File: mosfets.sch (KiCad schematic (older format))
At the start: 45 parts, among them Q1 ZXTC2045E6, Q10 ZXTC2045E6, Q11 IXFK230N20T, Q12 IXFK230N20T, Q2 ZXTC2045E6, Q3 IXFK230N20T, Q4 IXFK230N20T, Q5 ZXTC2045E6, Q6 ZXTC2045E6, Q7 IXFK230N20T, Q8 IXFK230N20T, Q9 ZXTC2045E6

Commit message: ~ changed gate resistance to 1R ~ changed power mosfet to IRFP4668PBF
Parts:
- Q11, Q12, Q3, Q4, Q7, Q8: value IXFK230N20T -> IRFP4668PBF
- R16, R17, R22, R23, R28, R29: value 4R7 -> 1R
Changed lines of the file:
@@
 LIBS:contrib
 LIBS:valves
-LIBS:alexlib
 LIBS:HSWR V2-cache
 EELAYER 25 0
@@
 P 9550 4750
 F 0 "R29" V 9630 4750 50  0000 C CNN
-F 1 "4R7" V 9550 4750 50  0000 C CNN
+F 1 "1R" V 9550 4750 50  0000 C CNN
 F 2 "Resistors_SMD:R_0805" V 9480 4750 50  0001 C CNN
 F 3 "" H 9550 4750 50  0000 C CNN
@@
 P 9550 2600
 F 0 "R28" V 9630 2600 50  0000 C CNN
-F 1 "4R7" V 9550 2600 50  0000 C CNN
+F 1 "1R" V 9550 2600 50  0000 C CNN
 F 2 "Resistors_SMD:R_0805" V 9480 2600 50  0001 C CNN
 F 3 "" H 9550 2600 50  0000 C CNN
@@
 P 9950 4750
 F 0 "Q12" H 10250 4800 50  0000 R CNN
-F 1 "IXFK230N20T" H 10600 4700 50  0000 R CNN
+F 1 "IRFP4668PBF" H 10600 4700 50  0000 R CNN
 F 2 "alexmod:TO-264_flat_reverse" H 10150 4850 29  0001 C CNN
 F 3 "" H 9950 4750 60  0000 C CNN
@@
 P 9950 2600
 F 0 "Q11" H 10250 2650 50  0000 R CNN
-F 1 "IXFK230N20T" H 10600 2550 50  0000 R CNN
+F 1 "IRFP4668PBF" H 10600 2550 50  0000 R CNN
 F 2 "alexmod:TO-264_flat_reverse" H 10150 2700 29  0001 C CNN
 F 3 "" H 9950 2600 60  0000 C CNN
@@
 P 6100 4750
 F 0 "R23" V 6180 4750 50  0000 C CNN
-F 1 "4R7" V 6100 4750 50  0000 C CNN
+F 1 "1R" V 6100 4750 50  0000 C CNN
 F 2 "Resistors_SMD:R_0805" V 6030 4750 50  0001 C CNN
 F 3 "" H 6100 4750 50  0000 C CNN
@@
 P 6100 2600
 F 0 "R22" V 6180 2600 50  0000 C CNN
-F 1 "4R7" V 6100 2600 50  0000 C CNN
+F 1 "1R" V 6100 2600 50  0000 C CNN
 F 2 "Resistors_SMD:R_0805" V 6030 2600 50  0001 C CNN
 F 3 "" H 6100 2600 50  0000 C CNN
@@
 P 6500 4750
 F 0 "Q8" H 6800 4800 50  0000 R CNN
-F 1 "IXFK230N20T" H 7150 4700 50  0000 R CNN
+F 1 "IRFP4668PBF" H 7150 4700 50  0000 R CNN
 F 2 "alexmod:TO-264_flat_reverse" H 6700 4850 29  0001 C CNN
 F 3 "" H 6500 4750 60  0000 C CNN
@@
 P 6500 2600
 F 0 "Q7" H 6800 2650 50  0000 R CNN
-F 1 "IXFK230N20T" H 7150 2550 50  0000 R CNN
+F 1 "IRFP4668PBF" H 7150 2550 50  0000 R CNN
 F 2 "alexmod:TO-264_flat_reverse" H 6700 2700 29  0001 C CNN
 F 3 "" H 6500 2600 60  0000 C CNN
@@
 P 2700 4750
 F 0 "R17" V 2780 4750 50  0000 C CNN
-F 1 "4R7" V 2700 4750 50  0000 C CNN
+F 1 "1R" V 2700 4750 50  0000 C CNN
 F 2 "Resistors_SMD:R_0805" V 2630 4750 50  0001 C CNN
 F 3 "" H 2700 4750 50  0000 C CNN
@@
 P 2700 2600
 F 0 "R16" V 2780 2600 50  0000 C CNN
-F 1 "4R7" V 2700 2600 50  0000 C CNN
+F 1 "1R" V 2700 2600 50  0000 C CNN
 F 2 "Resistors_SMD:R_0805" V 2630 2600 50  0001 C CNN
 F 3 "" H 2700 2600 50  0000 C CNN
@@
 P 3050 4750
 F 0 "Q4" H 3350 4800 50  0000 R CNN
-F 1 "IXFK230N20T" H 3700 4700 50  0000 R CNN
+F 1 "IRFP4668PBF" H 3700 4700 50  0000 R CNN
 F 2 "alexmod:TO-264_flat_reverse" H 3250 4850 29  0001 C CNN
 F 3 "" H 3050 4750 60  0000 C CNN
@@
 P 3050 2600
 F 0 "Q3" H 3350 2650 50  0000 R CNN
-F 1 "IXFK230N20T" H 3700 2550 50  0000 R CNN
+F 1 "IRFP4668PBF" H 3700 2550 50  0000 R CNN
 F 2 "alexmod:TO-264_flat_reverse" H 3250 2700 29  0001 C CNN
 F 3 "" H 3050 2600 60  0000 C CNN

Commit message: - updated project to 5.0.0 - added ignore file
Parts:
- C3, C4, C5, C52, C54, C55, C56, C57, C58, C6, C7, C8: symbol C -> Device:C
- C50, C51, C53: symbol CP -> Device:CP
- Q1, Q10, Q2, Q5, Q6, Q9: symbol ZXTC2045E6 -> HSWR-V2-rescue:ZXTC2045E6
- Q11, Q12, Q3, Q4, Q7, Q8: symbol Q_NMOS_GDS -> Device:Q_NMOS_GDS
- R12, R13, R14, R15, R16, R17, R18, R19, R20, R21, R22, R23, R24, R25, R26, R27, R28, R29: symbol R -> Device:R
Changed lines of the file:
@@
-EESchema Schematic File Version 2
-LIBS:HSWR V2-rescue
-LIBS:power
-LIBS:device
-LIBS:transistors
-LIBS:conn
-LIBS:linear
-LIBS:regul
-LIBS:74xx
-LIBS:cmos4000
-LIBS:adc-dac
-LIBS:memory
-LIBS:xilinx
-LIBS:microcontrollers
-LIBS:dsp
-LIBS:microchip
-LIBS:analog_switches
-LIBS:motorola
-LIBS:texas
-LIBS:intel
-LIBS:audio
-LIBS:interface
-LIBS:digital-audio
-LIBS:philips
-LIBS:display
-LIBS:cypress
-LIBS:siliconi
-LIBS:opto
-LIBS:atmel
-LIBS:contrib
-LIBS:valves
+EESchema Schematic File Version 4
 LIBS:HSWR V2-cache
-EELAYER 25 0
+EELAYER 26 0
 EELAYER END
 $Descr A4 11693 8268
@@
 Connection ~ 10050 3650
 $Comp
-L +BATT #PWR024
+L power:+BATT #PWR024
 U 1 1 575A4EA5
 P 10050 1700
@@
 $EndComp
 $Comp
-L R R29
+L Device:R R29
 U 1 1 57621E05
 P 9550 4750
@@
 	9750 4750 9700 4750
 $Comp
-L C C8
+L Device:C C8
 U 1 1 57621E21
 P 8200 5250
@@
 $EndComp
 $Comp
-L R R27
+L Device:R R27
 U 1 1 57621E27
 P 9350 5200
@@
 $EndComp
 $Comp
-L ZXTC2045E6 Q10
+L HSWR-V2-rescue:ZXTC2045E6 Q10
 U 1 1 57621E2D
 P 8800 4850
@@
 	8350 4400 8350 5050
 $Comp
-L R R25
+L Device:R R25
 U 1 1 57621E3C
 P 8600 4400
@@
 	10050 5400 10050 4950
 $Comp
-L R R28
+L Device:R R28
 U 1 1 576296B6
 P 9550 2600
@@
 Connection ~ 10050 3250
 $Comp
-L C C7
+L Device:C C7
 U 1 1 576296D2
 P 8200 3100
@@
 $EndComp
 $Comp
-L R R26
+L Device:R R26
 U 1 1 576296D8
 P 9350 3050
@@
 $EndComp
 $Comp
-L ZXTC2045E6 Q9
+L HSWR-V2-rescue:ZXTC2045E6 Q9
 U 1 1 576296DE
 P 8800 2700
@@
 	8350 2250 8350 2900
 $Comp
-L R R24
+L Device:R R24
 U 1 1 576296ED
 P 8600 2250
@@
 Connection ~ 8200 5400
 $Comp
-L Q_NMOS_GDS Q12
+L Device:Q_NMOS_GDS Q12
 U 1 1 57637BFB
 P 9950 4750
@@
 $EndComp
 $Comp
-L Q_NMOS_GDS Q11
+L Device:Q_NMOS_GDS Q11
 U 1 1 57637E5A
 P 9950 2600
@@
 Connection ~ 6600 3650
 $Comp
-L +BATT #PWR025
+L power:+BATT #PWR025
 U 1 1 589857E2
 P 6600 1700
@@
 $EndComp
 $Comp
-L R R23
+L Device:R R23
 U 1 1 589857E8
 P 6100 4750
@@
 	6300 4750 6250 4750
 $Comp
-L C C6
+L Device:C C6
 U 1 1 589857F0
 P 4750 5250
@@
 $EndComp
 $Comp
-L R R21
+L Device:R R21
 U 1 1 589857F7
 P 5900 5200
@@
 $EndComp
 $Comp
-L ZXTC2045E6 Q6
+L HSWR-V2-rescue:ZXTC2045E6 Q6
 U 1 1 589857FE
 P 5350 4850
@@
 	4900 4400 4900 5050
 $Comp
-L R R19
+L Device:R R19
 U 1 1 58985809
 P 5150 4400
@@
 	6600 5400 6600 4950
 $Comp
-L R R22
+L Device:R R22
 U 1 1 58985817
 P 6100 2600
@@
 Connection ~ 6600 3250
 $Comp
-L C C5
+L Device:C C5
 U 1 1 58985820
 P 4750 3100
@@
 $EndComp
 $Comp
-L R R20
+L Device:R R20
 U 1 1 58985827
 P 5900 3050
@@
 $EndComp
 $Comp
-L ZXTC2045E6 Q5
+L HSWR-V2-rescue:ZXTC2045E6 Q5
 U 1 1 5898582E
 P 5350 2700
@@
 	4900 2250 4900 2900
 $Comp
-L R R18
+L Device:R R18
 U 1 1 5898583A
 P 5150 2250
@@
 Connection ~ 4750 5400
 $Comp
-L Q_NMOS_GDS Q8
+L Device:Q_NMOS_GDS Q8
 U 1 1 5898584D
 P 6500 4750
@@
 $EndComp
 $Comp
-L Q_NMOS_GDS Q7
+L Device:Q_NMOS_GDS Q7
 U 1 1 58985854
 P 6500 2600
@@
 Connection ~ 3150 3650
 $Comp
-L +BATT #PWR026
+L power:+BATT #PWR026
 U 1 1 58986AF5
 P 3150 1700
@@
 $EndComp
 $Comp
-L R R17
+L Device:R R17
 U 1 1 58986AFB
 P 2700 4750
@@
 	2850 4750 2850 4750
 $Comp
-L C C4
+L Device:C C4
 U 1 1 58986B03
 P 1350 5250
@@
 $EndComp
 $Comp
-L R R15
+L Device:R R15
 U 1 1 58986B0A
 P 2500 5200
@@
 $EndComp
 $Comp
-L ZXTC2045E6 Q2
+L HSWR-V2-rescue:ZXTC2045E6 Q2
 U 1 1 58986B11
 P 1950 4850
@@
 	1500 4400 1500 5050
 $Comp
-L R R13
+L Device:R R13
 U 1 1 58986B1C
 P 1750 4400
@@
 	3150 5400 3150 4950
 $Comp
-L R R16
+L Device:R R16
 U 1 1 58986B2A
 P 2700 2600
@@
 Connection ~ 3150 3250
 $Comp
-L C C3
+L Device:C C3
 U 1 1 58986B33
 P 1350 3100
@@
 $EndComp
 $Comp
-L R R14
+L Device:R R14
 U 1 1 58986B3A
 P 2500 3050
@@
 $EndComp
 $Comp
-L ZXTC2045E6 Q1
+L HSWR-V2-rescue:ZXTC2045E6 Q1
 U 1 1 58986B41
 P 1950 2700
@@
 	1500 2250 1500 2900
 $Comp
-L R R12
+L Device:R R12
 U 1 1 58986B4D
 P 1750 2250
@@
 Connection ~ 1350 5400
 $Comp
-L Q_NMOS_GDS Q4
+L Device:Q_NMOS_GDS Q4
 U 1 1 58986B60
 P 3050 4750
@@
 $EndComp
 $Comp
-L Q_NMOS_GDS Q3
+L Device:Q_NMOS_GDS Q3
 U 1 1 58986B67
 P 3050 2600
@@
 	1200 5400 3800 5400
 $Comp
-L +BATT #PWR027
+L power:+BATT #PWR027
 U 1 1 58A716A6
 P 3450 7000
@@
 $EndComp
 $Comp
-L C C52
+L Device:C C52
 U 1 1 58A7831F
 P 3550 5200
@@
 $EndComp
 $Comp
-L C C54
+L Device:C C54
 U 1 1 58A78A84
 P 3800 5200
@@
 Connection ~ 3800 5050
 $Comp
-L C C55
+L Device:C C55
 U 1 1 58A797A9
 P 7000 5200
@@
 $EndComp
 $Comp
-L C C56
+L Device:C C56
 U 1 1 58A797AF
 P 7250 5200
@@
 Connection ~ 7250 5050
 $Comp
-L C C57
+L Device:C C57
 U 1 1 58A799C2
 P 10450 5200
@@
 $EndComp
 $Comp
-L C C58
+L Device:C C58
 U 1 1 58A799C8
 P 10700 5200
@@
 Connection ~ 6600 1700
 $Comp
-L CP C51
+L Device:CP C51
 U 1 1 58A7B686
 P 3450 7150
@@
 $EndComp
 $Comp
-L CP C53
+L Device:CP C53
 U 1 1 58A7B84C
 P 3700 7150
@@
 $EndComp
 $Comp
-L CP C50
+L Device:CP C50
 U 1 1 58A7B8F0
 P 3200 7150
@@
 $EndComp
 $Comp
-L GNDPWR #PWR028
+L HSWR-V2-rescue:GNDPWR #PWR028
 U 1 1 58A7BA9C
 P 3450 7300

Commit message: - updated to VESC6 architecture - still some things to do in schematic
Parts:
- removed C3, C4, C5, C6, C7, C8: 1u, Capacitors_SMD:C_0805, symbol Device:C
- removed Q1, Q10, Q2, Q5, Q6, Q9: ZXTC2045E6, TO_SOT_Packages_SMD:SOT-23-6, symbol HSWR-V2-rescue:ZXTC2045E6
- removed R12, R13, R18, R19, R24, R25: 120R, Resistors_SMD:R_0805, symbol Device:R
- removed R14, R15, R20, R21, R26, R27: 10k, Resistors_SMD:R_0805, symbol Device:R
- C50, C51, C53: footprint alexmod:C_Radial_D22_P10 -> Capacitor_THT:CP_Radial_D22.0mm_P10.00mm_SnapIn
- C52, C54, C55, C56, C57, C58: footprint Capacitors_SMD:C_2220 -> Capacitor_SMD:C_2220_5650Metric
- Q11, Q12, Q3, Q4, Q7, Q8: value IRFP4668PBF -> IXFK300N20X3; footprint alexmod:TO-264_flat_reverse -> Package_TO_SOT_THT:TO-264-3_Horizontal_TabUp
- R16, R17, R22, R23, R28, R29: footprint Resistors_SMD:R_0805 -> Resistor_SMD:R_0805_2012Metric
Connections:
- net labels added: U, U_GH, U_GL, U_VP, U_VS, V, V_GH, V_GL, V_VP, V_VS, W, W_GH, W_GL, W_VP, W_VS
- net labels removed: GNDPWR, H1_HI, H1_LOW, H1_VL, H1_VS, H2_HI, H2_LOW, H2_VL, H2_VS, H3_HI, H3_LOW, H3_VL, H3_VS, M_H1, M_H2, M_H3, M_L1, M_L2, M_L3, PHASE_1, PHASE_2, PHASE_3
- wire segments 95 -> 50

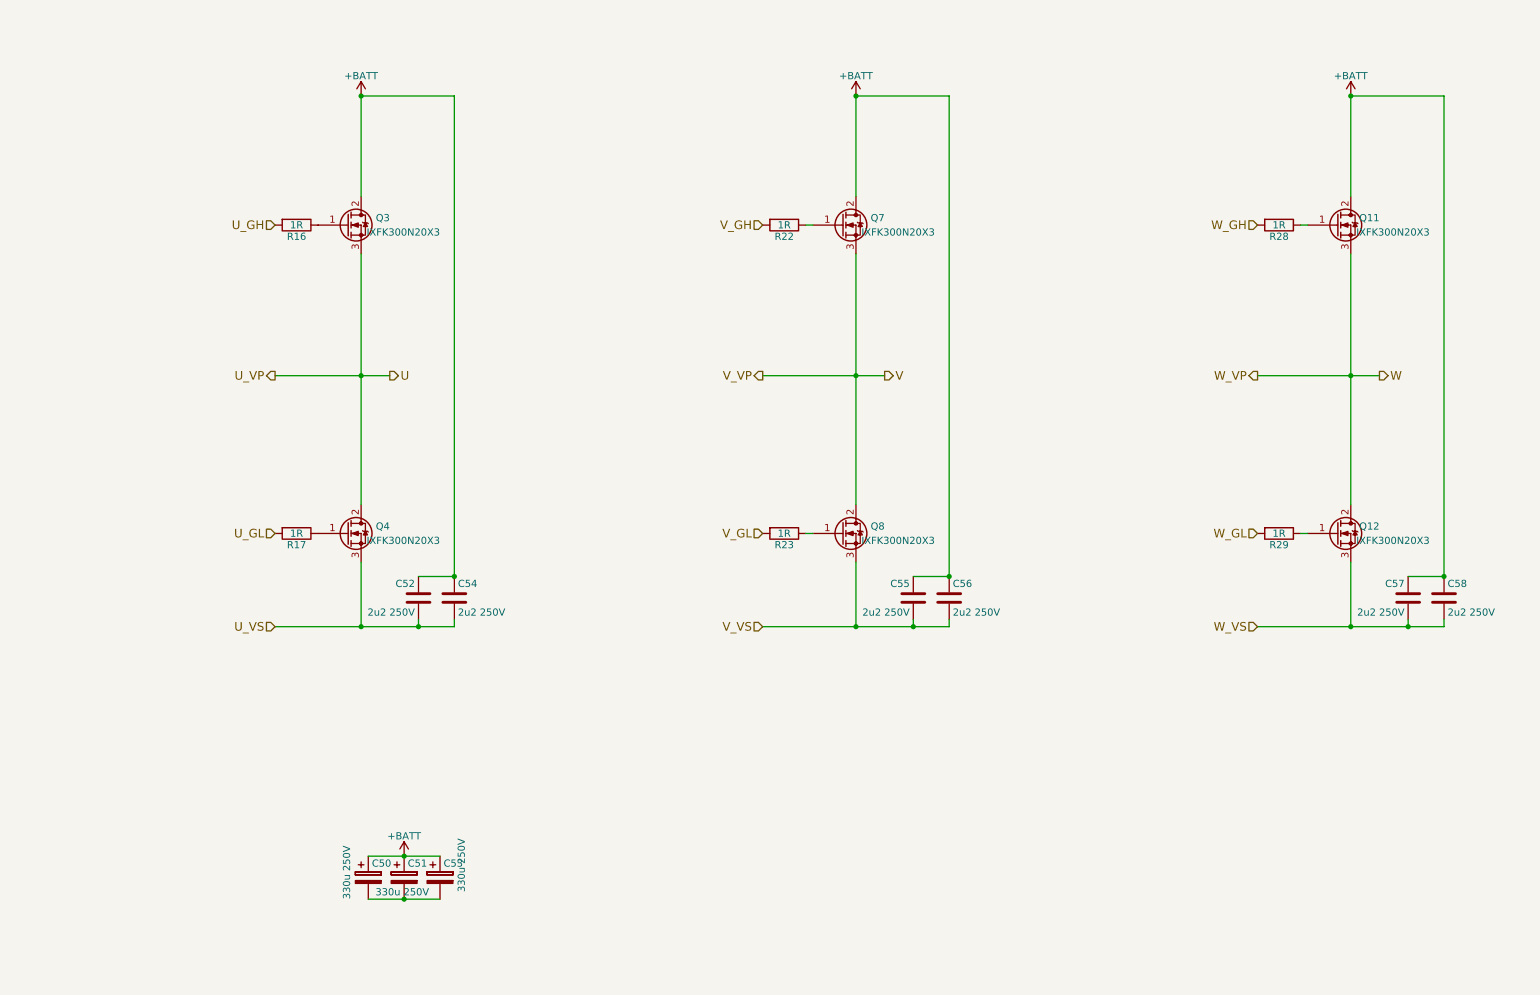
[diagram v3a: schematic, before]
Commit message: - started layout - high current path finished - some work on gate drivers
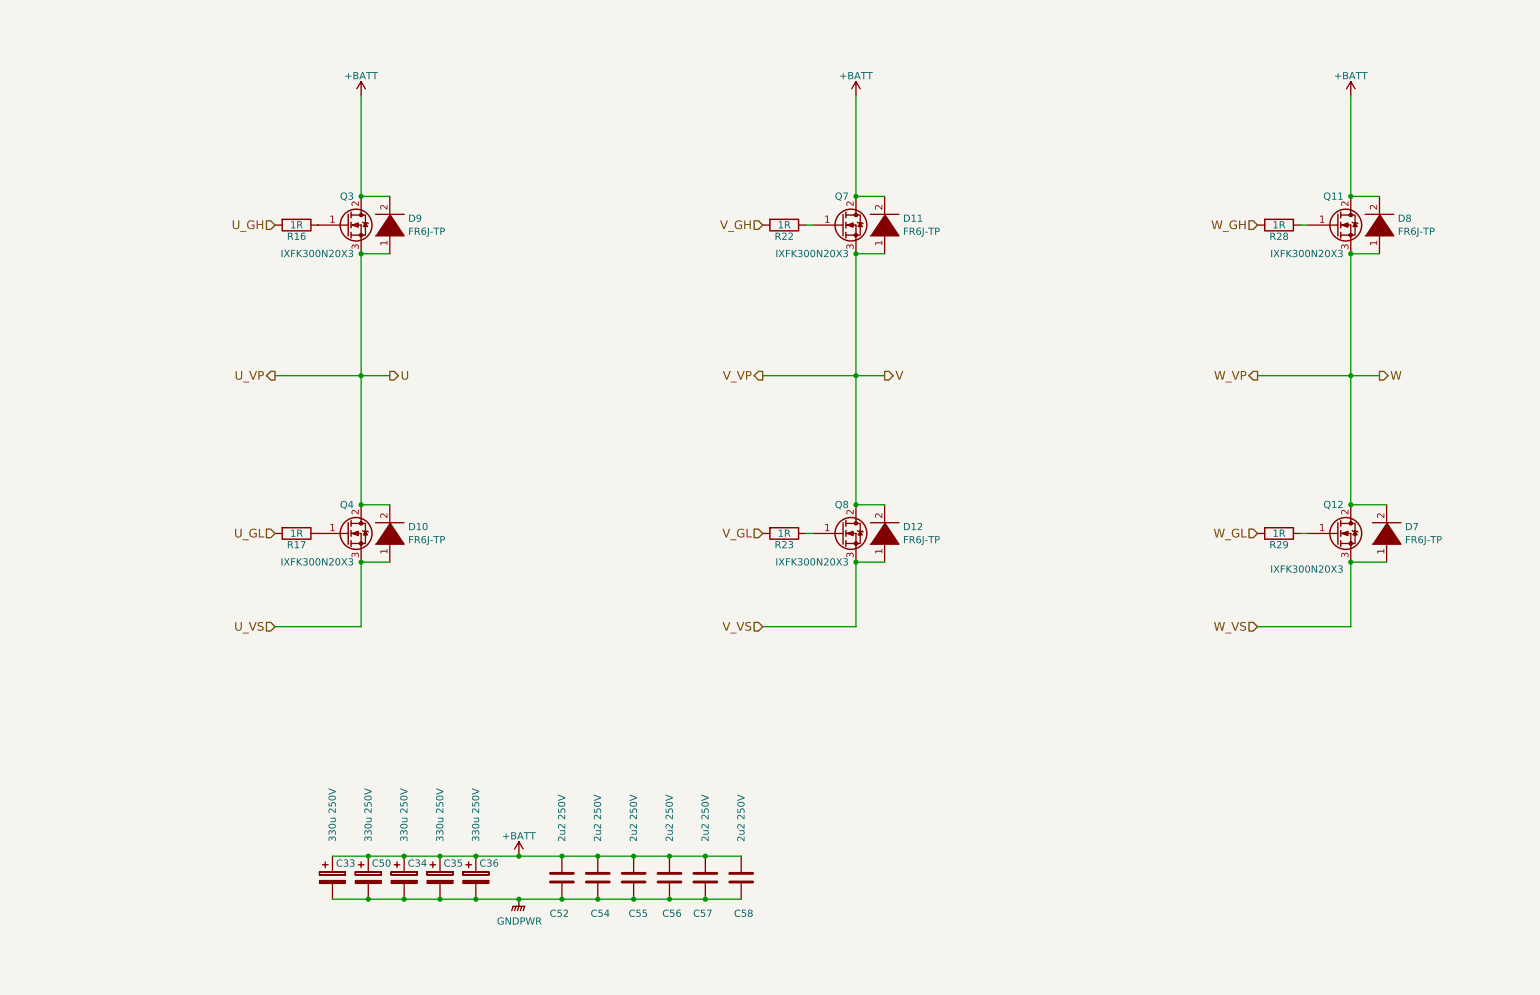
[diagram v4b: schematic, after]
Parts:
- removed C51, C53: 330u 250V, Capacitor_THT:CP_Radial_D22.0mm_P10.00mm_SnapIn, symbol Device:CP
- added C33, C34, C35, C36: 330u 250V, Capacitor_THT:CP_Radial_D22.0mm_P10.00mm_SnapIn, symbol Device:CP
- added D10, D11, D12, D7, D8, D9: FR6J-TP, Diode_SMD:D_SMC, symbol pspice:DIODE
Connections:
- net +BATT: now also C33.1, C34.1, C35.1, C36.1, D11.2 (A), D8.2 (A), D9.2 (A)
- net U: now also D10.2 (A), D9.1 (K)
- net U_VS: now also D10.1 (K); no longer C52.2, C54.2
- net V: now also D11.1 (K), D12.2 (A)
- net V_VS: now also D12.1 (K); no longer C55.2, C56.2
- net W: now also D7.2 (A), D8.1 (K)
- net W_VS: now also D7.1 (K); no longer C57.2, C58.2
- net GNDPWR: now reaches C50.2
- net GNDPWR: now also C52.2, C54.2, C55.2, C56.2, C57.2, C58.2, C33.2, C34.2, C35.2, C36.2
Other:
- moved on the sheet: C52, C54, C55, C56, C57, C58
